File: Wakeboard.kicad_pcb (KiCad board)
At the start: 2 copper layers, 30.6 x 58.6 mm, 34 parts, among them CN1 JST S2B-PH-SM4-TB(LF)(SN), J2 HCTL HC-TYPE-C-16P-01A, Q1 DMP2045UQ-7, SW1 TS-1088-AR02016, SW2 TS-1088-AR02016, U1 RT9080-33GJ5, U2 ESP32-S3-MINI-1, U3 LIS3DHTR_C15134, U4 MCP73831T-2ACI/OT

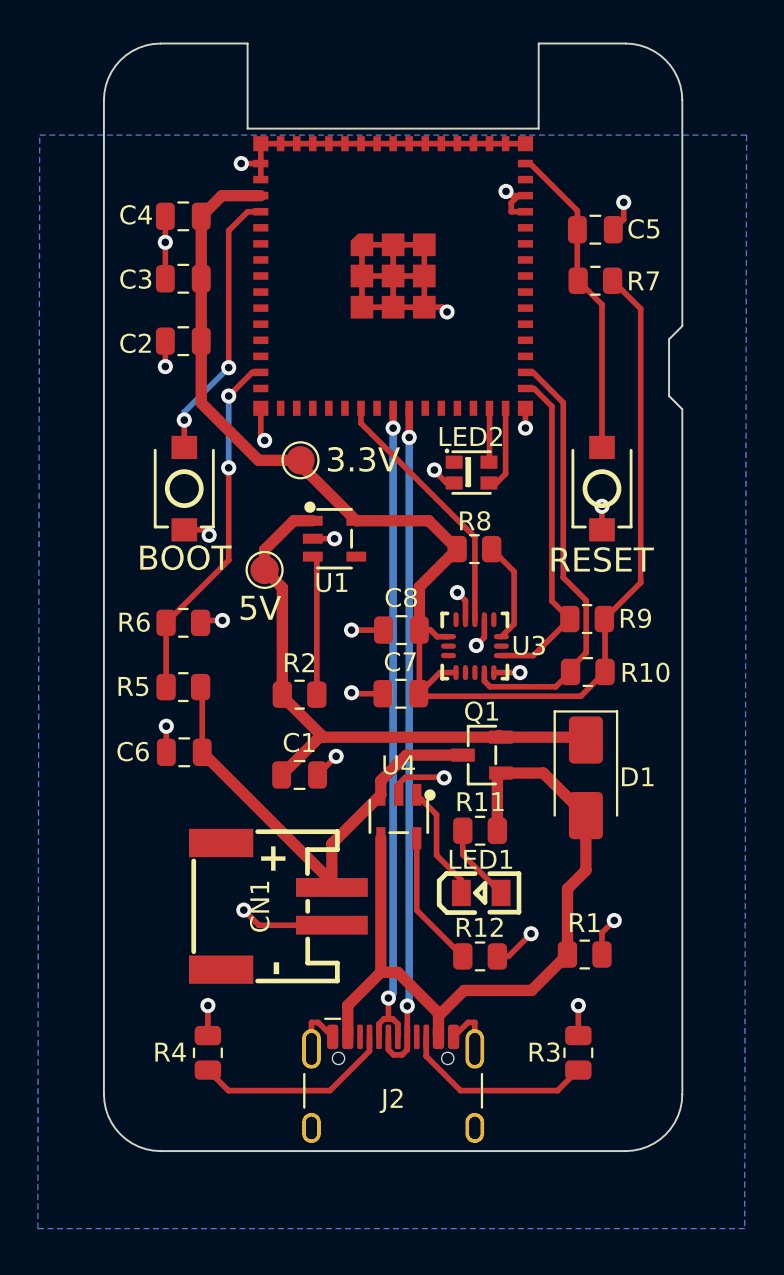
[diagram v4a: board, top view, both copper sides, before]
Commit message: Resize board
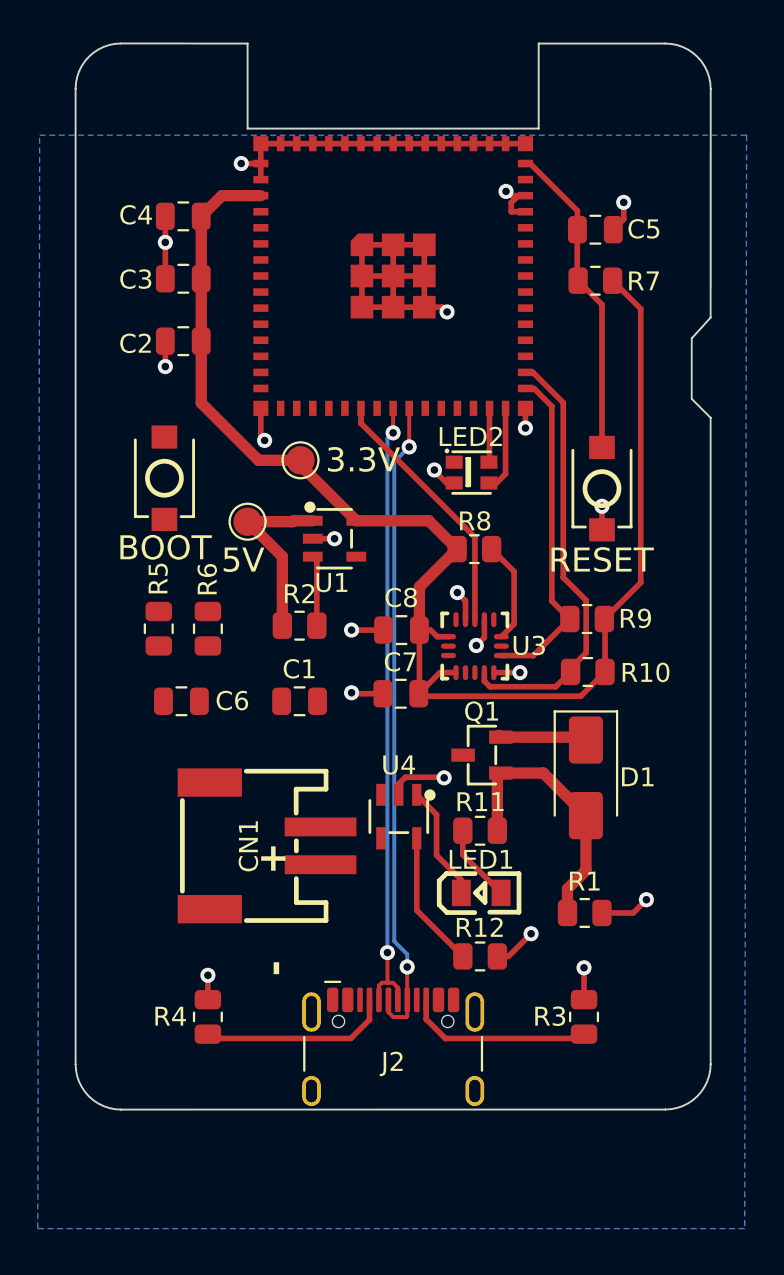
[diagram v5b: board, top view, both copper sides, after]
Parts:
- moved C1 3.90 mm to (122.5, 78.8)
- moved R2 3.65 mm to (122.5, 74.8)
- moved R5 3.35 mm to (115.1, 75.0), turned to -90 degrees
- moved CN1 3.26 mm to (120.7, 86.5)
- moved C6 2.70 mm to (116.3, 78.8), turned to 0 degrees
- moved TP1 2.70 mm to (119.8, 69.3)
- moved R1 2.20 mm to (137.6, 90.0)
- moved J2 1.95 mm to (127.5, 98.3)
- moved R3 1.92 mm to (137.6, 95.5)
- moved R4 1.90 mm to (117.7, 95.5)
- moved R6 1.34 mm to (117.7, 75.0), turned to 90 degrees
- moved SW1 1.19 mm to (115.4, 67.0)
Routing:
- net VBUS: track 40.9 -> 14.1 mm
- net VBAT: track 25.1 -> 0.00 mm
- net BAT_SENS: track 19.0 -> 0.00 mm, vias 2 -> 0
- net Net-(D1-K): track 31.5 -> 14.4 mm
- net GND: track 88.6 -> 72.9 mm, vias 26 -> 21
- net BOOT: track 14.6 -> 0.00 mm, vias 2 -> 0
- net Net-(U1-EN): track 7.39 -> 3.74 mm
- net D-: track 35.0 -> 33.1 mm
- net D+: track 35.9 -> 34.5 mm
- net Net-(J2-CC1): track 10.6 -> 10.1 mm
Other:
- board size 30.6 x 58.6 mm -> 33.6 x 56.4 mm

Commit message: Shift components after resize
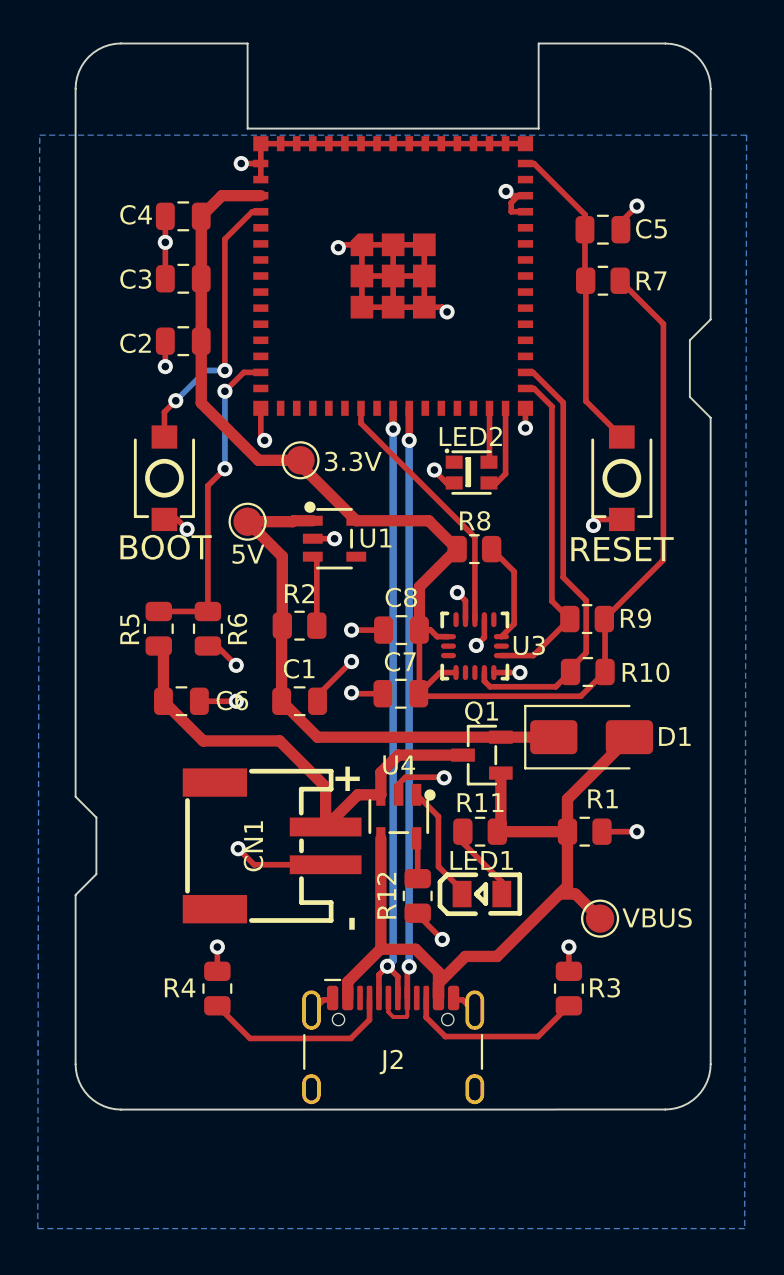
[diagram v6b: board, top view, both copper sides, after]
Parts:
- added TP3: VBUS, TestPoint:TestPoint_Pad_D1.5mm, F.Cu at (138.4, 90.3)
- moved R12 4.60 mm to (128.8, 89.1), turned to -90 degrees
- moved R1 4.30 mm to (137.6, 85.7)
- moved D1 2.17 mm to (138.0, 80.7), turned to 0 degrees
- moved R3 1.70 mm to (136.8, 94.0)
- moved R4 1.58 mm to (118.2, 94.0)
- moved SW2 1.19 mm to (139.6, 67.0)
- moved C5 0.40 mm to (138.6, 53.9)
- moved R7 0.40 mm to (138.6, 56.5)
- moved CN1 0.27 mm to (121.0, 86.5)
- moved J2 0.10 mm to (127.5, 98.2)
- moved LED1 0.07 mm to (132.2, 89.0)
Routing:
- net VBUS: track 14.1 -> 42.7 mm
- net VBAT: track 0.00 -> 25.1 mm
- net BAT_SENS: track 0.00 -> 16.9 mm, vias 0 -> 2
- net GND: track 72.9 -> 88.9 mm, vias 21 -> 27
- net BOOT: track 0.00 -> 14.9 mm, vias 0 -> 2
- net Net-(D1-K): track 14.4 -> 28.9 mm
- net Net-(U4-PROG): track 7.26 -> 2.16 mm
- net 3.3V: track 75.6 -> 76.7 mm
- net D+: track 34.5 -> 33.9 mm
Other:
- outline, holes or cut-outs redrawn

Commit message: Production files for latest PCB
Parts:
- moved J2 0.25 mm to (127.5, 98.0)
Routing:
- net VBUS: track 42.7 -> 44.0 mm
- net D-: track 33.4 -> 32.7 mm
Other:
- outline, holes or cut-outs redrawn
